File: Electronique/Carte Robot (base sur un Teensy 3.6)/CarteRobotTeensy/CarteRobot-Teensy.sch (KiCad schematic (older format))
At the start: 17 parts, among them J1 Teensy-3.6, J2 Conn_Bat2, J3 Conn_Bat1, J4 Conn_OnOff, J5 Conn_Aru, U1 TSR_1-2450

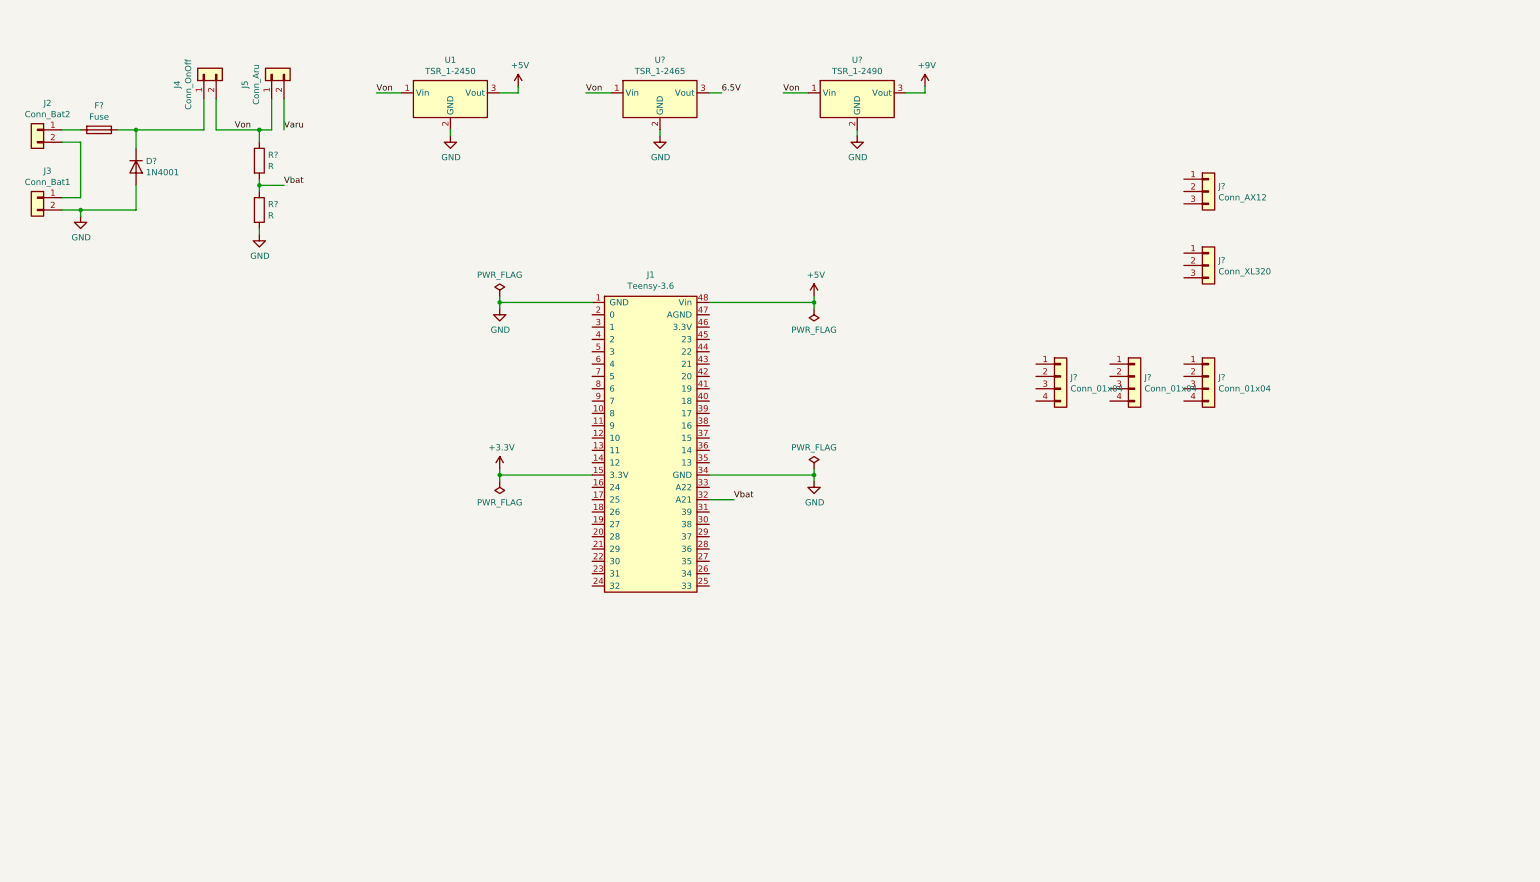
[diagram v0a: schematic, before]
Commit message: ajout driver schema de la carte
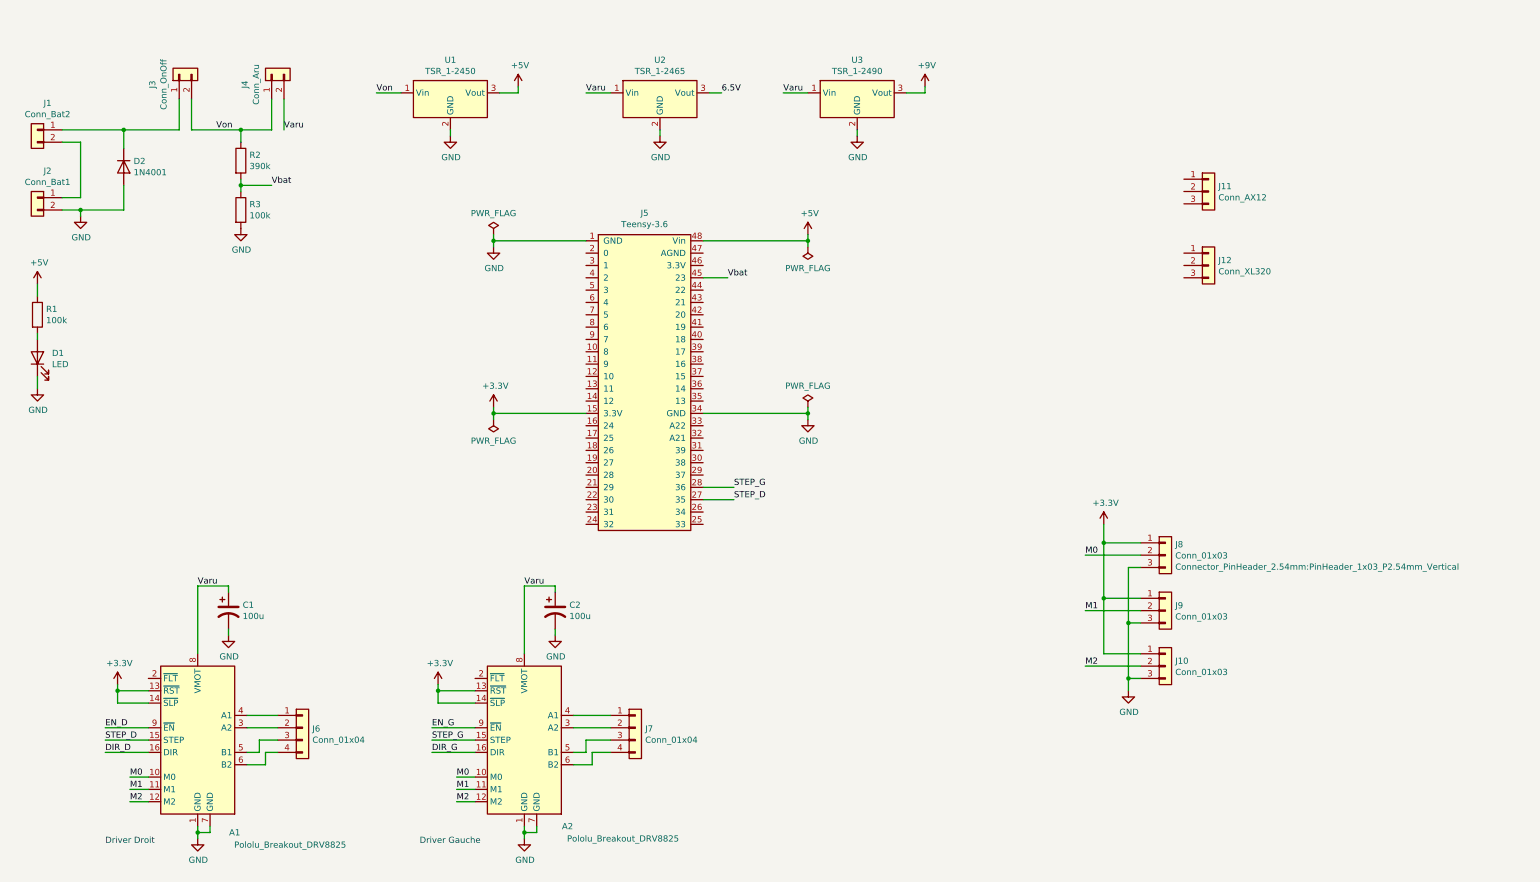
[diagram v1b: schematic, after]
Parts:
- removed F?: Fuse, symbol Device:Fuse
- removed J? (x3): Conn_01x04, symbol Connector_Generic:Conn_01x04
- added A1, A2: Pololu_Breakout_DRV8825, Module:Pololu_Breakout-16_15.2x20.3mm, symbol Driver_Motor:Pololu_Breakout_DRV8825
- added C1, C2: 100u, symbol Device:CP1
- added D1: LED, symbol Device:LED
- added J10, J8, J9: Conn_01x03, Connector_PinHeader_2.54mm:PinHeader_1x03_P2.54mm_Vertical, symbol Connector_Generic:Conn_01x03
- added J6, J7: Conn_01x04, symbol Connector_Generic:Conn_01x04
- added R1: 100k, symbol Device:R
- J1: renamed from J2; footprint (none) -> Mes_empreintes:SL_3.50-02-180G_Weidmuller
- J11: renamed from J?; footprint (none) -> Connector_Molex:Molex_SPOX_5267-03A_1x03_P2.50mm_Vertical
- J2: renamed from J3; footprint (none) -> Mes_empreintes:SL_3.50-02-180G_Weidmuller
- J3: renamed from J4; footprint (none) -> Connector_PinHeader_2.54mm:PinHeader_1x02_P2.54mm_Vertical
- J4: renamed from J5; footprint (none) -> Connector_PinHeader_2.54mm:PinHeader_1x02_P2.54mm_Vertical
- R2: renamed from R?; value R -> 390k
- R3: renamed from R?; value R -> 100k
- gave numbers to parts that had none: 4
- renumbered J1 to J5
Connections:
- net +3V3: now also A1.13 (~RST), A1.14 (~SLP), A2.13 (~RST), A2.14 (~SLP), J10.1 (Pin_1), J8.1 (Pin_1), J9.1 (Pin_1)
- net +5V: now also R1.1
- net GND: now also A1.1 (GND), A1.7 (GND), A2.1 (GND), A2.7 (GND), C1.2, C2.2, D1.1 (K), J10.3 (Pin_3), J8.3 (Pin_3), J9.3 (Pin_3)
- net Varu: now also U2.1 (Vin), U3.1 (Vin), A1.8 (VMOT), A2.8 (VMOT), C1.1, C2.1
- net Vbat: now also J5.45 (23); no longer J5.32 (A21)
- net Von: no longer U2.1 (Vin), U3.1 (Vin)
- net STEP_D: now reaches J5.27 (35)
- net STEP_D: now also A1.15 (STEP)
- net STEP_G: now reaches J5.28 (36)
- net STEP_G: now also A2.15 (STEP)
- net at D2.1 (K), J3.1 (Pin_1): now also J1.1 (Pin_1)
- new net: D1.2 (A), R1.2
- new net: A2.3 (A2), J7.2 (Pin_2)
- new net: A2.4 (A1), J7.1 (Pin_1)
- new net: A2.5 (B1), J7.3 (Pin_3)
- new net: A2.6 (B2), J7.4 (Pin_4)
- new net: A1.3 (A2), J6.2 (Pin_2)
- new net: A1.4 (A1), J6.1 (Pin_1)
- new net: A1.5 (B1), J6.3 (Pin_3)
- new net: A1.6 (B2), J6.4 (Pin_4)
- new net DIR_D: A1.16 (DIR)
- new net DIR_G: A2.16 (DIR)
- new net EN_D: A1.9 (~EN)
- new net EN_G: A2.9 (~EN)
- new net M0: A1.10 (M0), A2.10 (M0), J8.2 (Pin_2)
- new net M1: A1.11 (M1), A2.11 (M1), J9.2 (Pin_2)
- new net M2: A1.12 (M2), A2.12 (M2), J10.2 (Pin_2)
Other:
- note added: "Driver Droit"
- note added: "Driver Gauche"
- moved on the sheet: D2, J3, J5, R2, R3

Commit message: ajouts des connecteurs pour l'uart
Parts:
- added J13, J15, J16: Conn_01x04, Connector_Molex:Molex_KK-254_AE-6410-04A_1x04_P2.54mm_Vertical, symbol Connector_Generic:Conn_01x04
- added J14: Conn_01x03, Connector_PinHeader_2.54mm:PinHeader_1x03_P2.54mm_Vertical, symbol Connector_Generic:Conn_01x03
- J12: footprint (none) -> Connector_Molex:Molex_Micro-Latch_53253-0370_1x03_P2.00mm_Vertical
- J3, J4: footprint Connector_PinHeader_2.54mm:PinHeader_1x02_P2.54mm_Vertical -> Connector_Molex:Molex_KK-254_AE-6410-02A_1x02_P2.54mm_Vertical
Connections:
- net +3V3: now also J15.1 (Pin_1), J16.1 (Pin_1)
- net +9V: now also J11.2 (Pin_2), J14.1 (Pin_1)
- net 6.5V: now also J12.2 (Pin_2), J14.3 (Pin_3)
- net GND: now also J11.1 (Pin_1), J12.1 (Pin_1), J13.2 (Pin_2), J15.2 (Pin_2), J16.2 (Pin_2)
- net TX2: now reaches J5.10 (8)
- net TX2: now also J12.3 (Pin_3), J16.3 (Pin_3)
- net RX1: now reaches J5.2 (0)
- net TX1: now reaches J5.3 (1)
- net RX3: now reaches J5.7 (5)
- net RX3: now also J15.4 (Pin_4)
- net TX3: now reaches J5.8 (6)
- net TX3: now also J11.3 (Pin_3), J15.3 (Pin_3)
- net RX2: now reaches J5.9 (7)
- net RX2: now also J16.4 (Pin_4)
- new net: J13.1 (Pin_1), J14.2 (Pin_2)
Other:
- note added: "Driver Droite"
- note removed: "Driver Droit"

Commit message: ajouts connecteurs, leds
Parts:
- added J17, J18, J20, J21: Conn_01x04, Connector_Molex:Molex_KK-254_AE-6410-04A_1x04_P2.54mm_Vertical, symbol Connector_Generic:Conn_01x04
- added J19: Conn_01x03, Connector_Molex:Molex_KK-254_AE-6410-03A_1x03_P2.54mm_Vertical, symbol Connector_Generic:Conn_01x03
- C1, C2: footprint (none) -> Capacitor_THT:CP_Radial_D6.3mm_P2.50mm
- D1: footprint (none) -> LED_THT:LED_D5.0mm_Clear
- J6, J7: footprint (none) -> Connector_Molex:Molex_KK-254_AE-6410-04A_1x04_P2.54mm_Vertical
- R1: footprint (none) -> Resistor_SMD:R_0805_2012Metric_Pad1.20x1.40mm_HandSolder
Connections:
- net EN_D is gone; now on net EN: A1.9 (~EN)
- net EN_G is gone; now on net EN: A2.9 (~EN)
- net +3V3: now also J20.4 (Pin_4), J21.4 (Pin_4)
- net +5V: now also J17.1 (Pin_1), J18.1 (Pin_1)
- net DIR_D: now also J5.31 (39)
- net DIR_G: now also J5.28 (36)
- net GND: now also J17.2 (Pin_2), J18.2 (Pin_2), J20.3 (Pin_3), J21.3 (Pin_3)
- net STEP_D: now also J5.30 (38); no longer J5.27 (35)
- net STEP_G: now also J5.27 (35); no longer J5.28 (36)
- net Varu: now also J4.1 (Pin_1); no longer J4.2 (Pin_2)
- net Von: now also J3.1 (Pin_1), J4.2 (Pin_2); no longer J3.2 (Pin_2), J4.1 (Pin_1)
- net RX4: now reaches J5.23 (31)
- net RX4: now also J17.4 (Pin_4)
- net TX4: now reaches J5.24 (32)
- net TX4: now also J17.3 (Pin_3)
- net TX5: now reaches J5.25 (33)
- net TX5: now also J18.3 (Pin_3)
- net RX5: now reaches J5.26 (34)
- net RX5: now also J18.4 (Pin_4)
- net EN: now reaches J5.29 (37)
- net SDA0: now reaches J5.40 (18)
- net SDA0: now also J20.2 (Pin_2), J21.2 (Pin_2)
- net SCL0: now reaches J5.41 (19)
- net SCL0: now also J20.1 (Pin_1), J21.1 (Pin_1)
- net 20: now reaches J5.42 (20)
- net 20: now also J19.3 (Pin_3)
- net 21: now reaches J5.43 (21)
- net 21: now also J19.2 (Pin_2)
- net 22: now reaches J5.44 (22)
- net 22: now also J19.1 (Pin_1)
- net at D2.1 (K), J1.1 (Pin_1): now also J3.2 (Pin_2); no longer J3.1 (Pin_1)
- net at A2.3 (A2): now also J7.4 (Pin_4); no longer J7.2 (Pin_2)
- net at J7.1 (Pin_1): now also A2.6 (B2); no longer A2.4 (A1)
- net at A2.5 (B1): now also J7.2 (Pin_2); no longer J7.3 (Pin_3)
- net at A1.3 (A2): now also J6.1 (Pin_1); no longer J6.2 (Pin_2)
- net A1D: now reaches A1.4 (A1)
- net A1D: now also J6.2 (Pin_2); no longer J6.1 (Pin_1)
- new net A1G: A2.4 (A1), J7.3 (Pin_3)
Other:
- moved on the sheet: D2, J6, J7

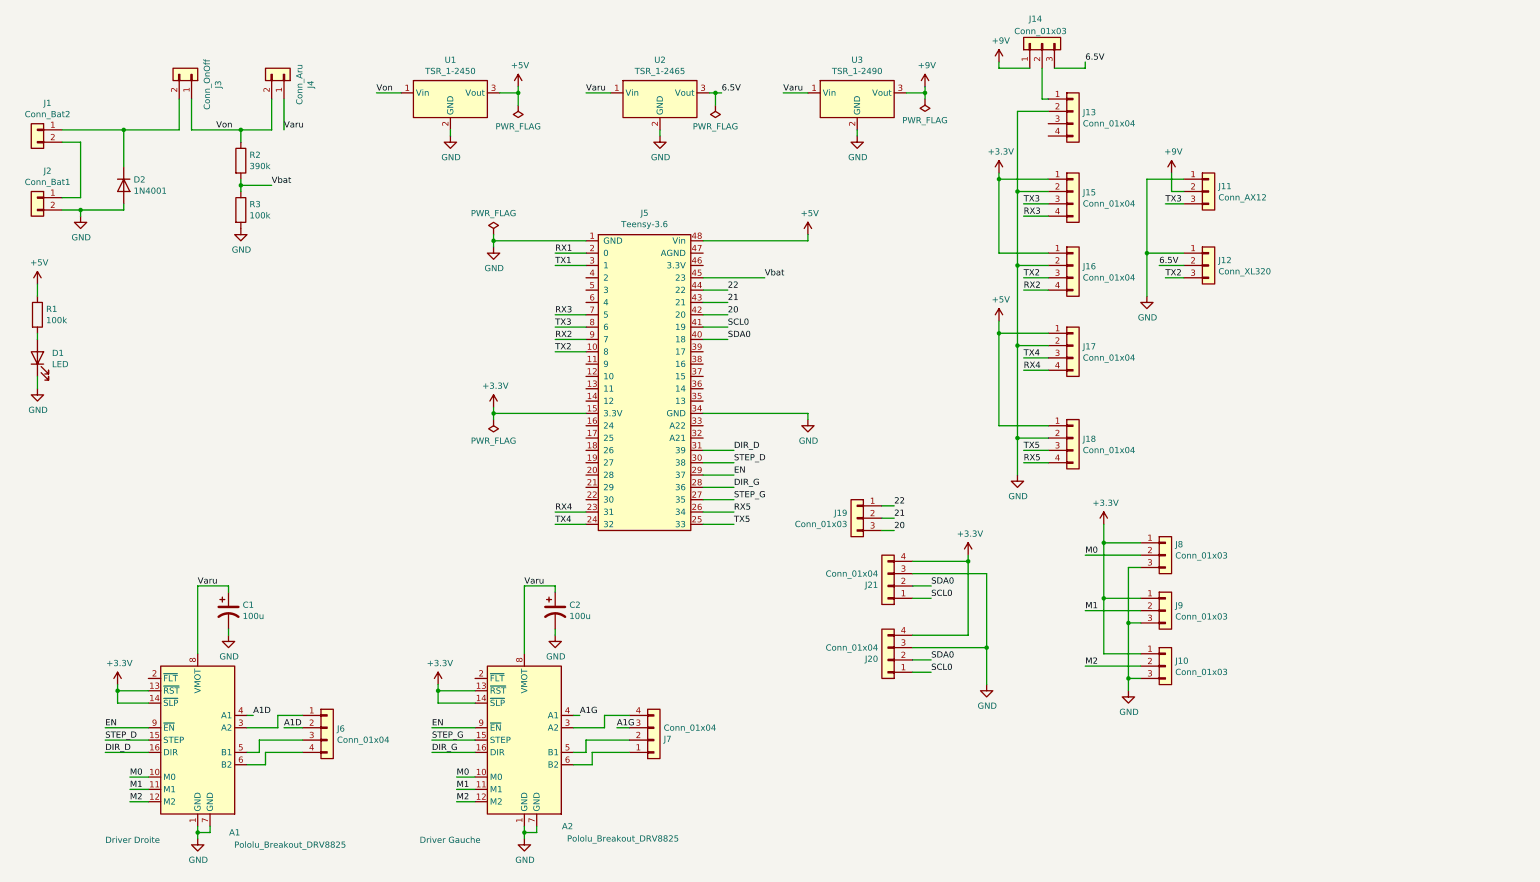
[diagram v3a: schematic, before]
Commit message: adaptateur servo Dynamixel + connecteur SPI
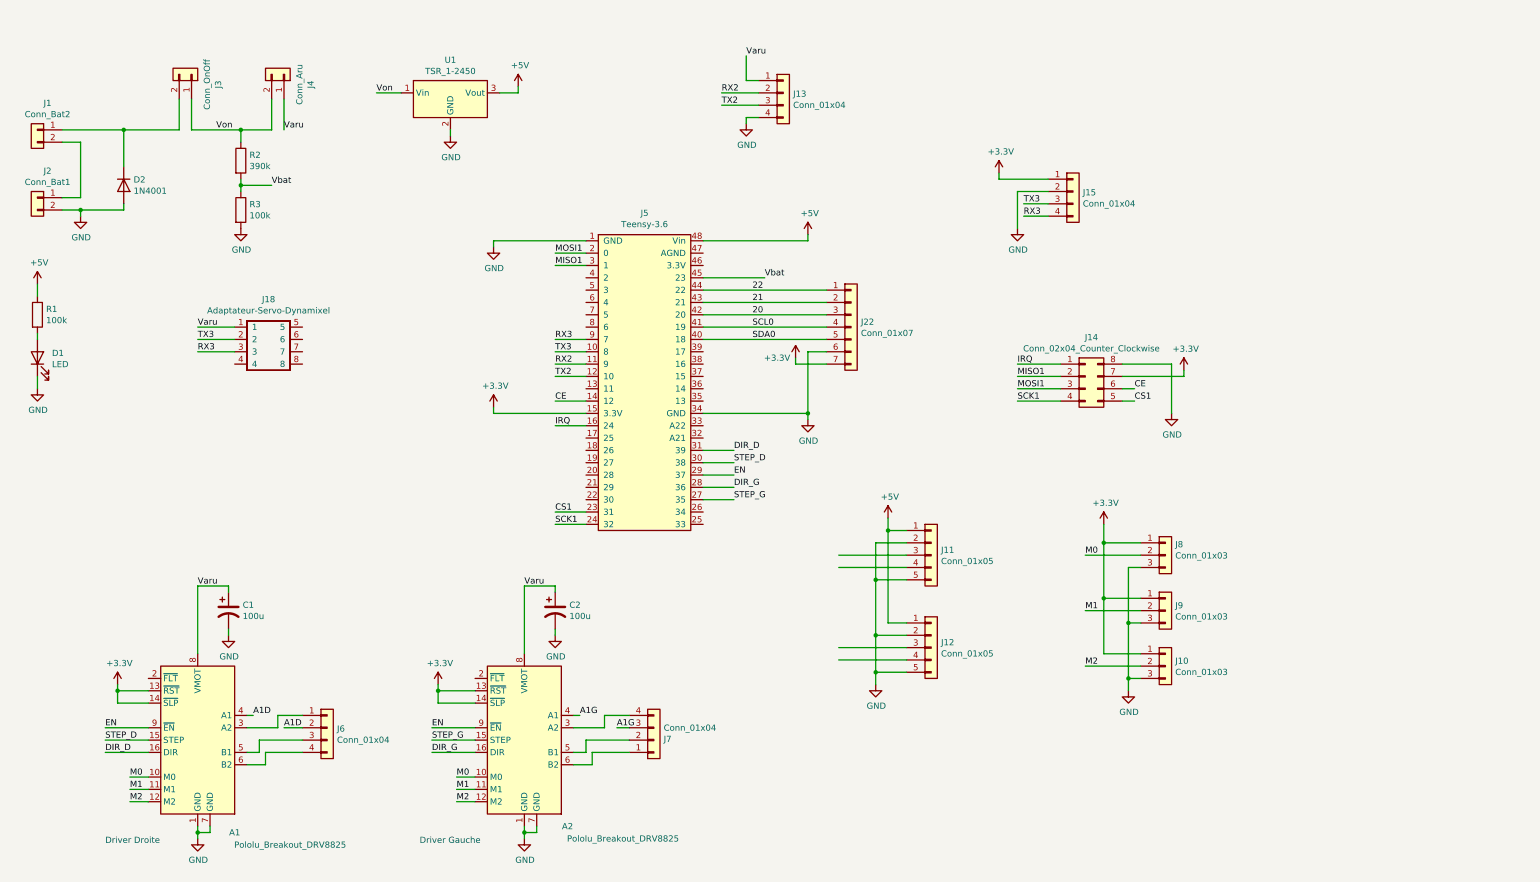
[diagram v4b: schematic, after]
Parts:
- removed J11: Conn_AX12, Connector_Molex:Molex_SPOX_5267-03A_1x03_P2.50mm_Vertical, symbol Connector_Generic:Conn_01x03
- removed J12: Conn_XL320, Connector_Molex:Molex_Micro-Latch_53253-0370_1x03_P2.00mm_Vertical, symbol Connector_Generic:Conn_01x03
- removed J14: Conn_01x03, Connector_PinHeader_2.54mm:PinHeader_1x03_P2.54mm_Vertical, symbol Connector_Generic:Conn_01x03
- removed J16, J17, J18, J20, J21: Conn_01x04, Connector_Molex:Molex_KK-254_AE-6410-04A_1x04_P2.54mm_Vertical, symbol Connector_Generic:Conn_01x04
- removed J19: Conn_01x03, Connector_Molex:Molex_KK-254_AE-6410-03A_1x03_P2.54mm_Vertical, symbol Connector_Generic:Conn_01x03
- removed U2: TSR_1-2465, Converter_DCDC:Converter_DCDC_TRACO_TSR-1_THT, symbol Regulator_Switching:TSR_1-2465
- removed U3: TSR_1-2490, Converter_DCDC:Converter_DCDC_TRACO_TSR-1_THT, symbol Regulator_Switching:TSR_1-2490
- added J11, J12: Conn_01x05, Connector_Molex:Molex_KK-254_AE-6410-05A_1x05_P2.54mm_Vertical, symbol Connector_Generic:Conn_01x05
- added J14: Conn_02x04_Counter_Clockwise, Connector_PinHeader_2.54mm:PinHeader_2x04_P2.54mm_Vertical, symbol Connector_Generic:Conn_02x04_Counter_Clockwise
- added J18: Adaptateur-Servo-Dynamixel, Mes_empreintes:Adaptateur-Servo-Dynamixel, symbol Mes_symboles:Adaptateur-Servo-Dynamixel
- added J22: Conn_01x07, Connector_Molex:Molex_KK-254_AE-6410-07A_1x07_P2.54mm_Vertical, symbol Connector_Generic:Conn_01x07
- R1: footprint Resistor_SMD:R_0805_2012Metric_Pad1.20x1.40mm_HandSolder -> Resistor_THT:R_Axial_DIN0207_L6.3mm_D2.5mm_P10.16mm_Horizontal
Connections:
- net +3V3: now also J14.7 (Pin_7), J22.7 (Pin_7)
- net +5V: now also J11.1 (Pin_1), J12.1 (Pin_1)
- net 20: now also J22.3 (Pin_3)
- net 21: now also J22.2 (Pin_2)
- net 22: now also J22.1 (Pin_1)
- net GND: now also J13.4 (Pin_4), J11.2 (Pin_2), J11.5 (Pin_5), J12.2 (Pin_2), J12.5 (Pin_5), J14.8 (Pin_8), J22.6 (Pin_6); no longer J13.2 (Pin_2)
- net RX2: now also J13.2 (Pin_2), J5.11 (9); no longer J5.9 (7)
- net RX3: now also J5.9 (7), J18.3; no longer J5.7 (5)
- net SCL0: now also J22.4 (Pin_4)
- net SDA0: now also J22.5 (Pin_5)
- net TX2: now also J13.3 (Pin_3), J5.12 (10); no longer J5.10 (8)
- net TX3: now also J5.10 (8), J18.2; no longer J5.8 (6)
- net Varu: now also J13.1 (Pin_1), J18.1
- net CE: now reaches J5.14 (12)
- net CE: now also J14.6 (Pin_6)
- net IRQ: now reaches J5.16 (24)
- net IRQ: now also J14.1 (Pin_1)
- net RX1 renamed MOSI1
- net MOSI1: now also J14.3 (Pin_3)
- net RX4 renamed CS1
- net CS1: now also J14.5 (Pin_5)
- net RX5: no longer names the net of J5.26 (34)
- net TX1 renamed MISO1
- net MISO1: now also J14.2 (Pin_2)
- net TX4 renamed SCK1
- net SCK1: now also J14.4 (Pin_4)
- net TX5: no longer names the net of J5.25 (33)
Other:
- moved on the sheet: J13
